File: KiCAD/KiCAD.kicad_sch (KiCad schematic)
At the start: 0 parts

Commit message: schematic: I2C topology flip + CD14538B heartbeat + pre-layout audit
- Documentation updates for the STEMMA-QT topology flip (MCP4728 upstream
  of Si5351): design_review_7-5-26 C1 marked resolved, build_checklist
  Phase 1 gets the 6-step first-boot procedure, cw_envelope_keyer I2C
  address section rewritten, front_panel_interface signal-chain diagram
  refreshed.
- CD14538B dual retriggerable monostable added to xmitter.kicad_sym
  (PDIP-16, pinout verified against datasheet fig. 1), plus datasheet
  file.
- Arduino sheet: CD14538B heartbeat topology on Q5 HV contactor -- U18
  + R30 470K + C41 1uF timing (t_w ~470 ms), Q7 series FET stack,
  C42/C43 VDD bypass and bulk.
- Pre-layout audit output as Documentation/punch_list_7-6-26.txt (list
  of blockers before PCB layout, ordered by severity).

Co-Authored-By: Claude Opus 4.7 (1M context) <noreply@anthropic.com>
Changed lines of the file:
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@@
 			)
 		)
-		(pin "CS_DAC" input
+		(pin "CS_DAC" output
 			(at 85.09 59.69 270)
 			(effects
@@
 			)
 		)
-		(pin "MOSI" input
+		(pin "MOSI" output
 			(at 99.06 59.69 270)
 			(effects
@@
 			)
 		)
-		(pin "SCK" input
+		(pin "SCK" output
 			(at 96.52 59.69 270)
 			(effects

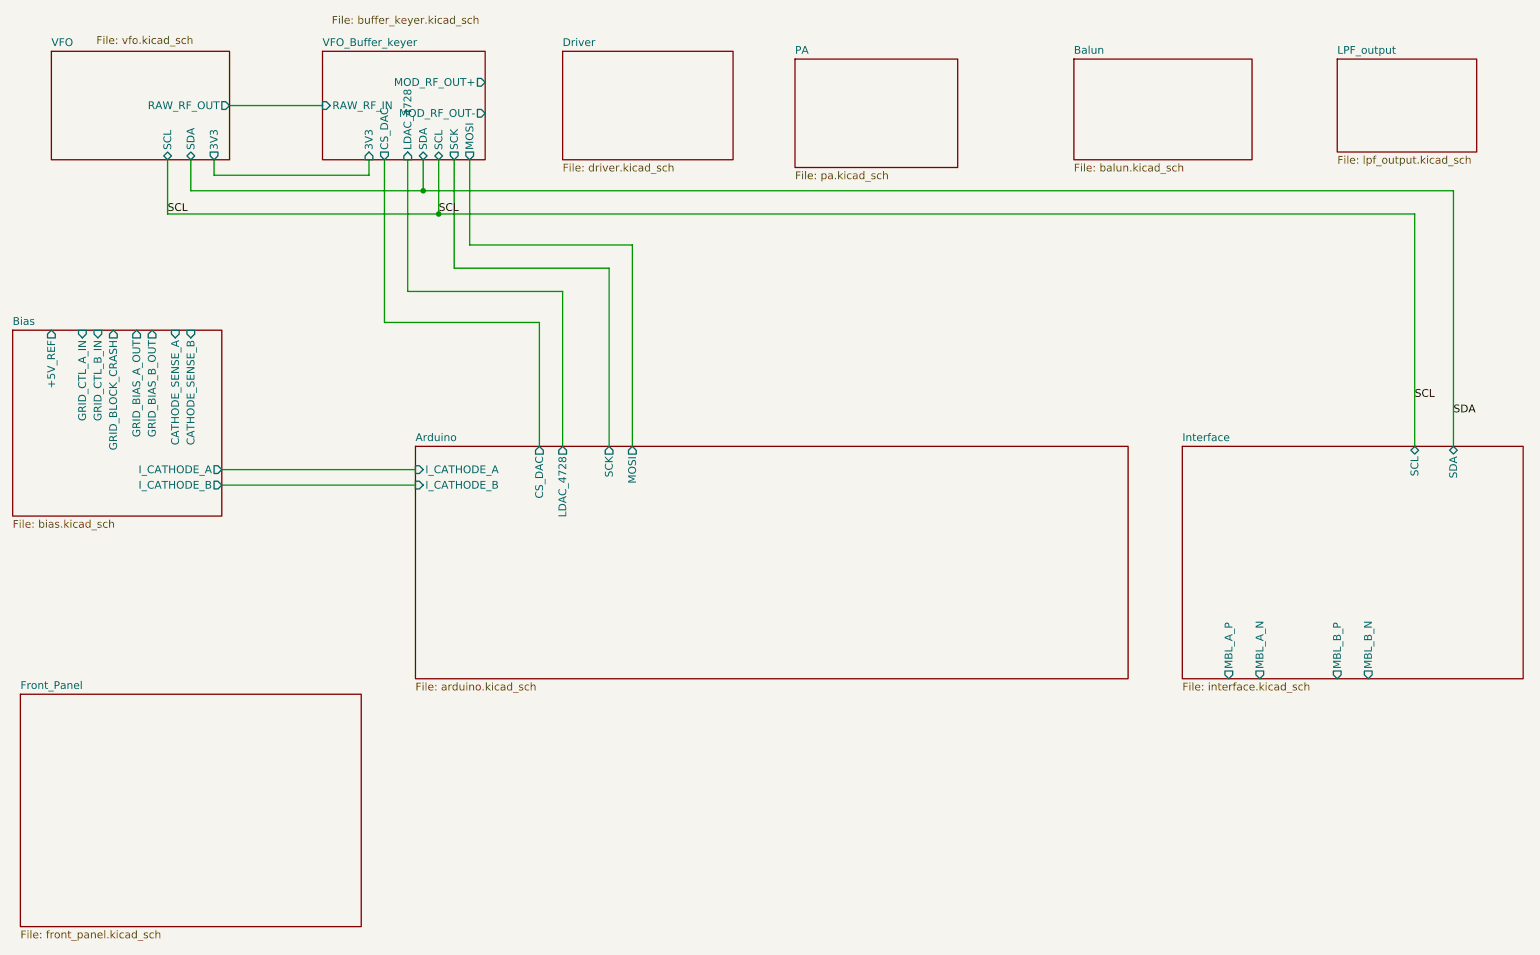
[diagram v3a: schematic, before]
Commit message: kicad: convert hierarchical labels to globals (Path A) + unify _OUT/_IN pairs
- 58 hierarchical_label -> global_label conversions across the six active
  sheets. Standard KiCad 10 global_label form with fields_autoplaced +
  Intersheetrefs property.
- Stripped 36 vestigial sheet pins, 28 stitching wires, 2 junctions, 4
  labels from the root sheet. Sheet blocks remain; each is now a pure
  container with globals doing the cross-sheet connectivity by name.
- Renamed three OUT/IN pairs to unified names so same-name globals
  auto-connect:
    GRID_CTL_A_OUT + GRID_CTL_A_IN -> GRID_CTL_A
    GRID_CTL_B_OUT + GRID_CTL_B_IN -> GRID_CTL_B
    RAW_RF_OUT     + RAW_RF_IN     -> RAW_RF
- tools/convert_hier_to_global.py and tools/strip_root_stitching.py:
  reusable if we ever need to redo this.
- Documentation/punch_list_7-6-26.txt: mark B1a-e, L1, L2 resolved; add
  M6 (cosmetic) about GRID_CTL_A's label-at-pin-origin idiom; correct
  the earlier GRID_CTL_A false positive with the verified chain
  MCP4728 U8 VC -> R_PADA -> OPA454 U5 IN+ + Q3 drain.

Co-Authored-By: Claude Opus 4.7 (1M context) <noreply@anthropic.com>
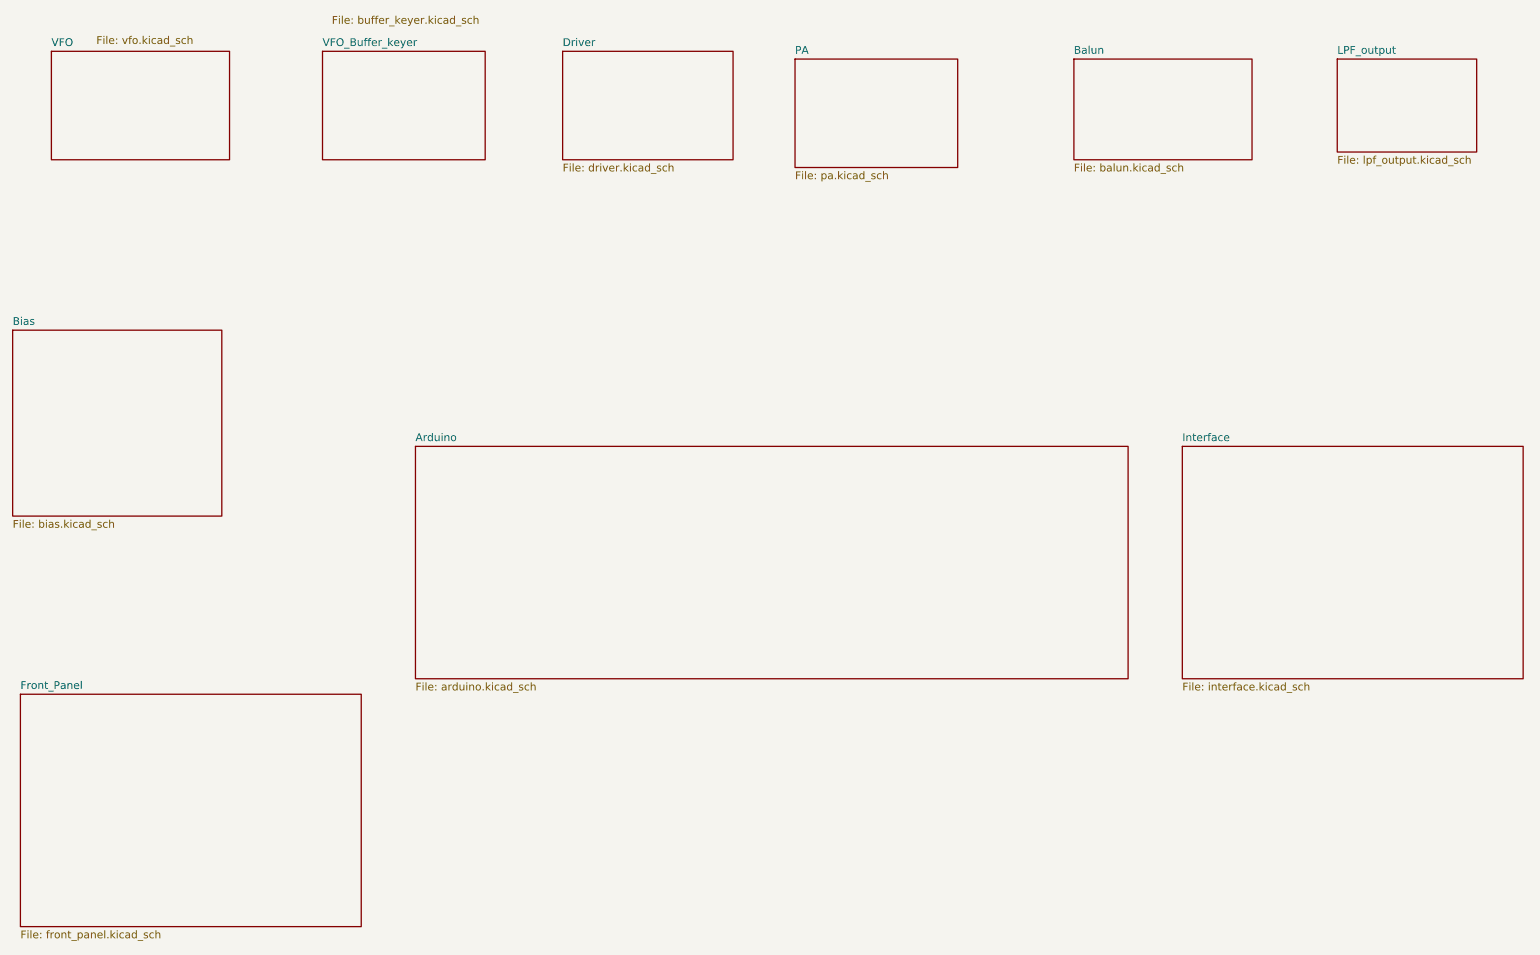
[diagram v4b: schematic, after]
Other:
- sheet Arduino ports: added none; removed CS_DAC, I_CATHODE_A, I_CATHODE_B, LDAC_4728, MOSI, SCK
- sheet Bias ports: added none; removed +5V_REF, CATHODE_SENSE_A, CATHODE_SENSE_B, GRID_BIAS_A_OUT, GRID_BIAS_B_OUT, GRID_BLOCK_CRASH, GRID_CTL_A_IN, GRID_CTL_B_IN, I_CATHODE_A, I_CATHODE_B
- sheet Interface ports: added none; removed MBL_A_N, MBL_A_P, MBL_B_N, MBL_B_P, SCL, SDA
- sheet VFO ports: added none; removed 3V3, RAW_RF_OUT, SCL, SDA
- sheet VFO_Buffer_keyer ports: added none; removed 3V3, CS_DAC, LDAC_4728, MOD_RF_OUT+, MOD_RF_OUT-, MOSI, RAW_RF_IN, SCK, SCL, SDA

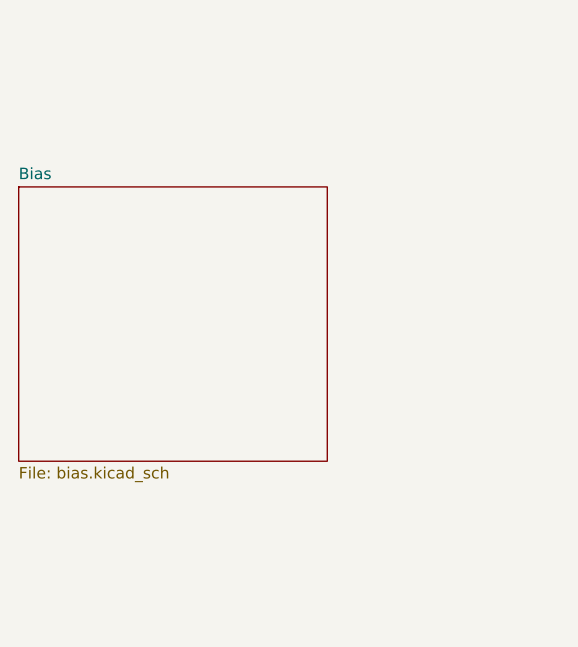
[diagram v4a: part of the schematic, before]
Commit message: kicad: L79L08 local decoupling; unlink bias sheet from root
- Add C17/C18 (0.33 uF Z5U SR205E334MAR) at L79L08 in/out to prevent
  oscillation and damp L7+U19 ringing
- New footprint xmitter:Kyocera_SR20_MLCC for the SR20 style radial MLCC
  (2.54 mm pitch, 5.08 x 3.175 mm body)
- Add SR-Series datasheet to Documentation/Components
- Unlink bias sheet from root schematic — first step in splitting the
  bias circuit onto its own PCB

Co-Authored-By: Claude Opus 4.7 <noreply@anthropic.com>
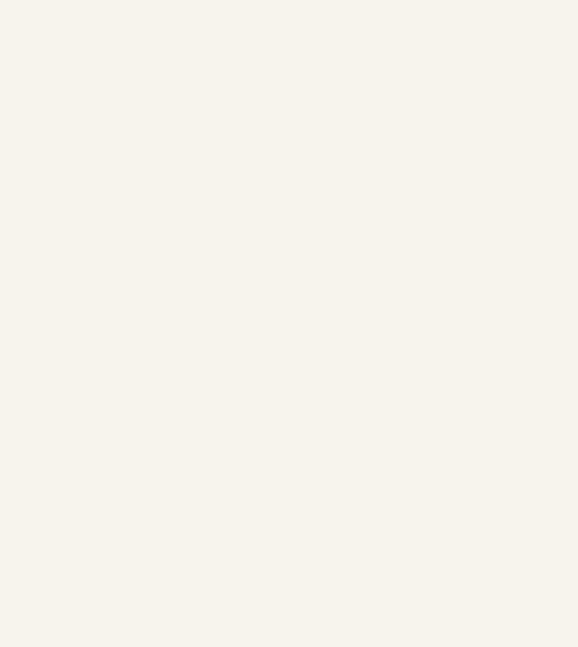
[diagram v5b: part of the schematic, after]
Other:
- removed sheet Bias
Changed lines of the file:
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@@
-	)
-	(sheet
-		(at 24.13 87.63)
-		(size 34.29 30.48)
-		(exclude_from_sim no)
-		(in_bom yes)
-		(on_board yes)
-		(dnp no)
-		(fields_autoplaced yes)
-		(stroke
-			(width 0.1524)
-			(type solid)
-		)
-		(fill
-			(color 0 0 0 0)
-		)
-		(property "Sheetname" "Bias"
-			(at 24.13 86.9184 0)
-			(show_name no)
-			(do_not_autoplace no)
-			(effects
-				(font
-					(size 1.27 1.27)
-				)
-				(justify left bottom)
-			)
-		)
-		(property "Sheetfile" "bias.kicad_sch"
-			(at 24.13 118.6946 0)
-			(show_name no)
-			(do_not_autoplace no)
-			(effects
-				(font
-					(size 1.27 1.27)
-				)
-				(justify left top)
-			)
-		)
-		(instances
-			(project "KiCAD"
-				(path "/d3de40b8-856b-4fbd-829c-f45ffcd55742"
-					(page "9")
-				)
-			)
-		)
 	)
 	(sheet
